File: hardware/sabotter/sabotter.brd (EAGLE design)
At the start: 92.5 x 80 mm, 111 parts, among them IC1 MAX3232CSE, IC2 MAX3232CSE, IC3 OKI-78SR-3.3/1.5-W36H-C, IC4 OKI-78SR-5/1.5-W36H-C, IC6 ATXMEGA256A3U-AU, IC7 LM4871M

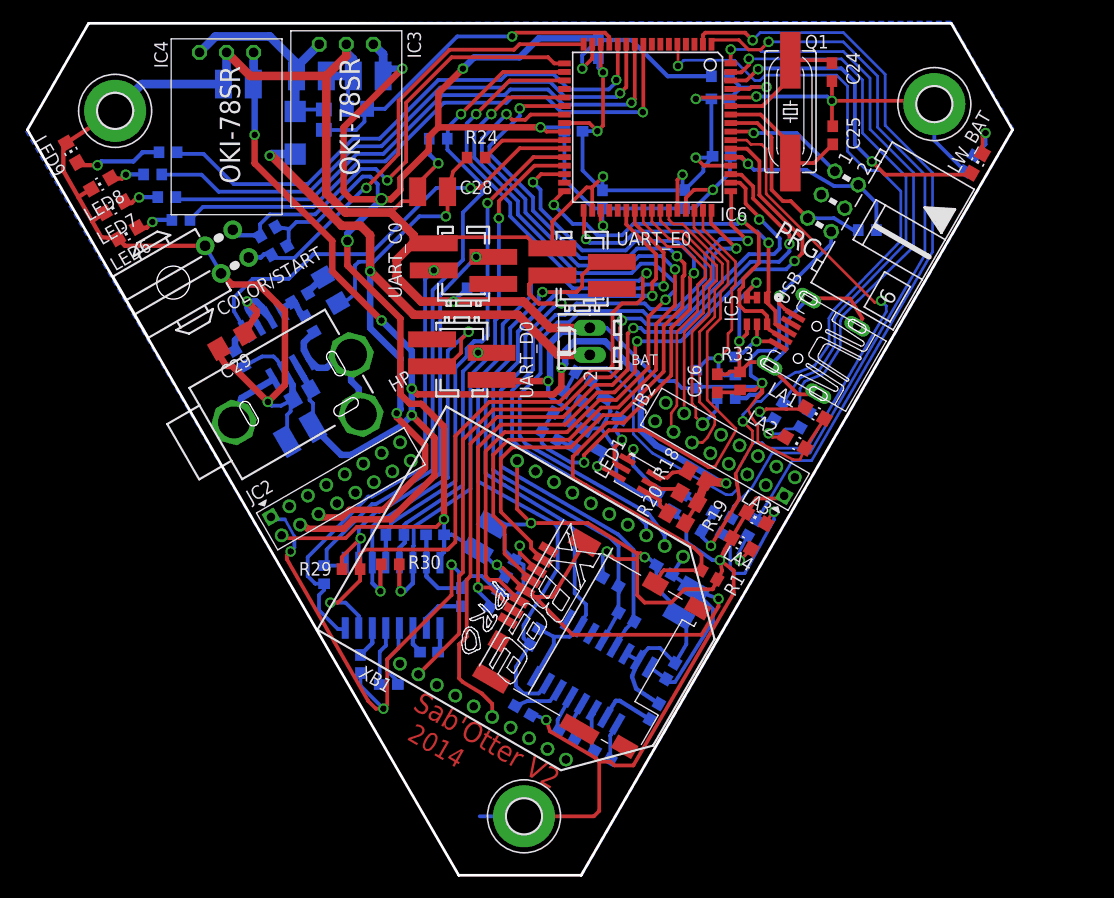
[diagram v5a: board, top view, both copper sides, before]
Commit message: sabotter: uart modified after Jdam  peer review
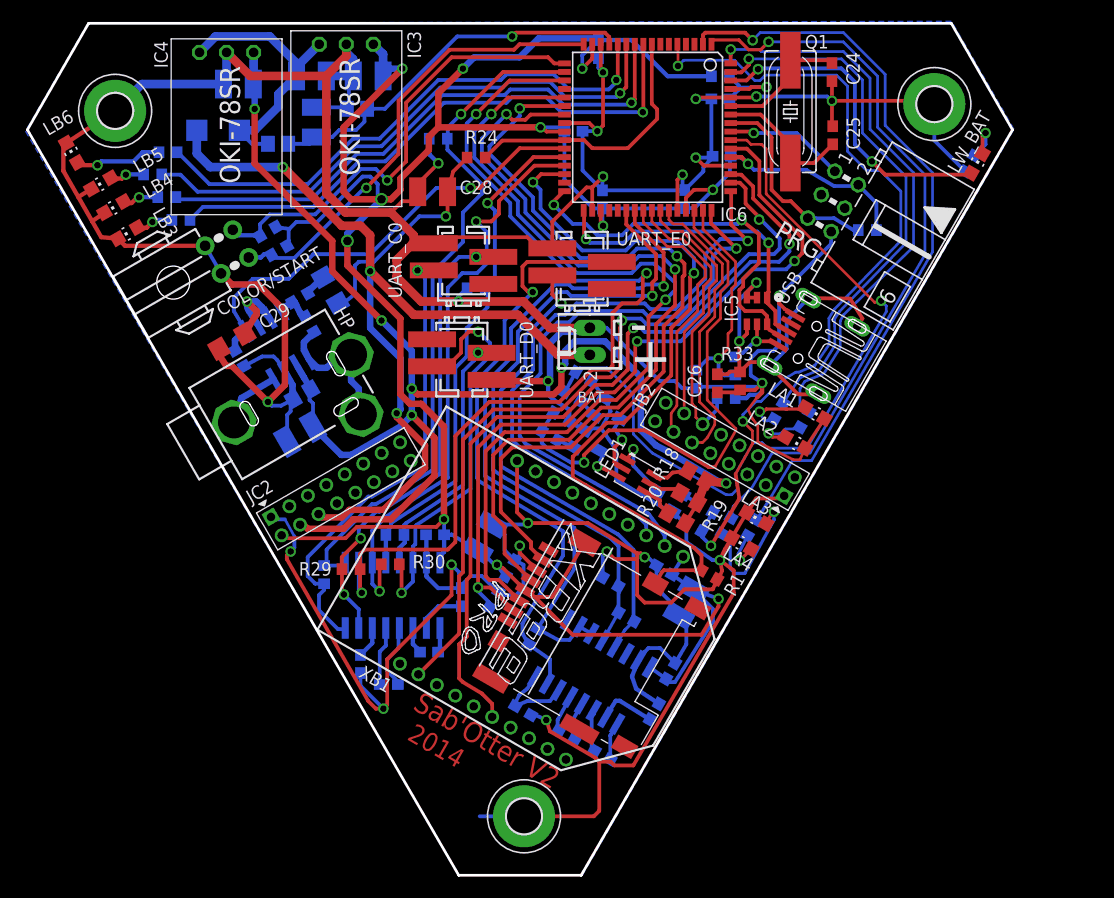
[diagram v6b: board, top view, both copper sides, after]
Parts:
- added C32: C_10UF, robotter_capacitor:C1210
- R24: value 10K-F -> 470
- R33: value (none) -> 10M
- T1, T2, T3: value (none) -> 2n2222
- moved D1 7.24 mm to (17.9, 70.0), turned to 0 degrees
- moved R23 4.87 mm to (23.5, 68.7), turned to 0 degrees
- moved R31 0.12 mm to (47.5, 22.4), turned to 120 degrees
- turned R30 to 180 degrees
- renumbered LED6 to LB3, LED7 to LB4, LED8 to LB5, LED9 to LB6
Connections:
- removed net N$19: C10.1, IC1.6
- removed net PD4: JB2.9
- removed net PD5: JB2.10
- removed net PD6: JB2.8
- removed net PD7: JB2.7
- new net V-: C10.1, IC1.6, IC1.8
- net AUDIO_PWM_3V3: now also IC6.8
- net GND: now also C32.2; no longer IC1.14
- net TX_C0_232: now also IC2.7; no longer IC2.10
- net TX_C0_3V3: now also IC2.10; no longer IC2.7
- net TX_D0_232: now also IC2.14; no longer IC2.11
- net TX_D0_3V3: now also IC2.11; no longer IC2.14
- net TX_E0_232: now also IC1.7; no longer IC1.10, IC1.8
- net TX_E0_3V3: now also IC1.10, IC1.11; no longer IC1.7
- net VBAT_0_1V: now also C32.1
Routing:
- net AUDIO_PWM_3V3: track 8.13 -> 25.5 mm
- net V-: track 0.00 -> 8.50 mm
- net +12V: track 75.4 -> 81.9 mm
- net N$62: track 22.0 -> 27.2 mm
- net TX_E0_3V3: track 70.7 -> 65.7 mm
- net TX_C0_232: track 41.1 -> 46.0 mm, vias 2 -> 3
- net N$19: track 4.65 -> 0.00 mm
- net RX_E0_232: track 49.6 -> 45.4 mm
- net VBAT_0_1V: track 32.0 -> 35.9 mm
- net TX_C0_3V3: track 95.1 -> 91.3 mm
- net TX_D0_3V3: track 51.4 -> 55.2 mm
- net GND: track 583.1 -> 584.8 mm
- net TX_E0_232: track 55.8 -> 57.4 mm
- net TX_D0_232: track 37.5 -> 38.3 mm
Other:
- board text added: "+"
- board text added: "-"

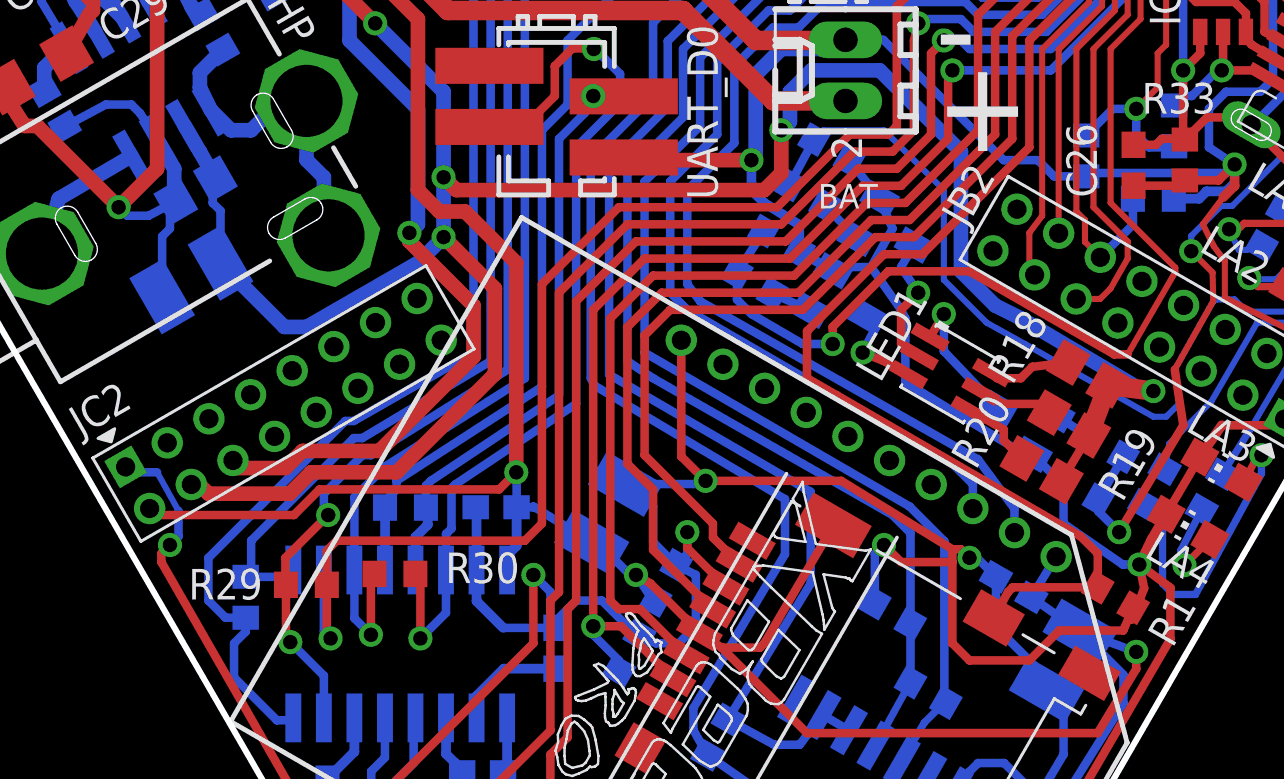
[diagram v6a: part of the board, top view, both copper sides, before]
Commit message: radiospares part number added
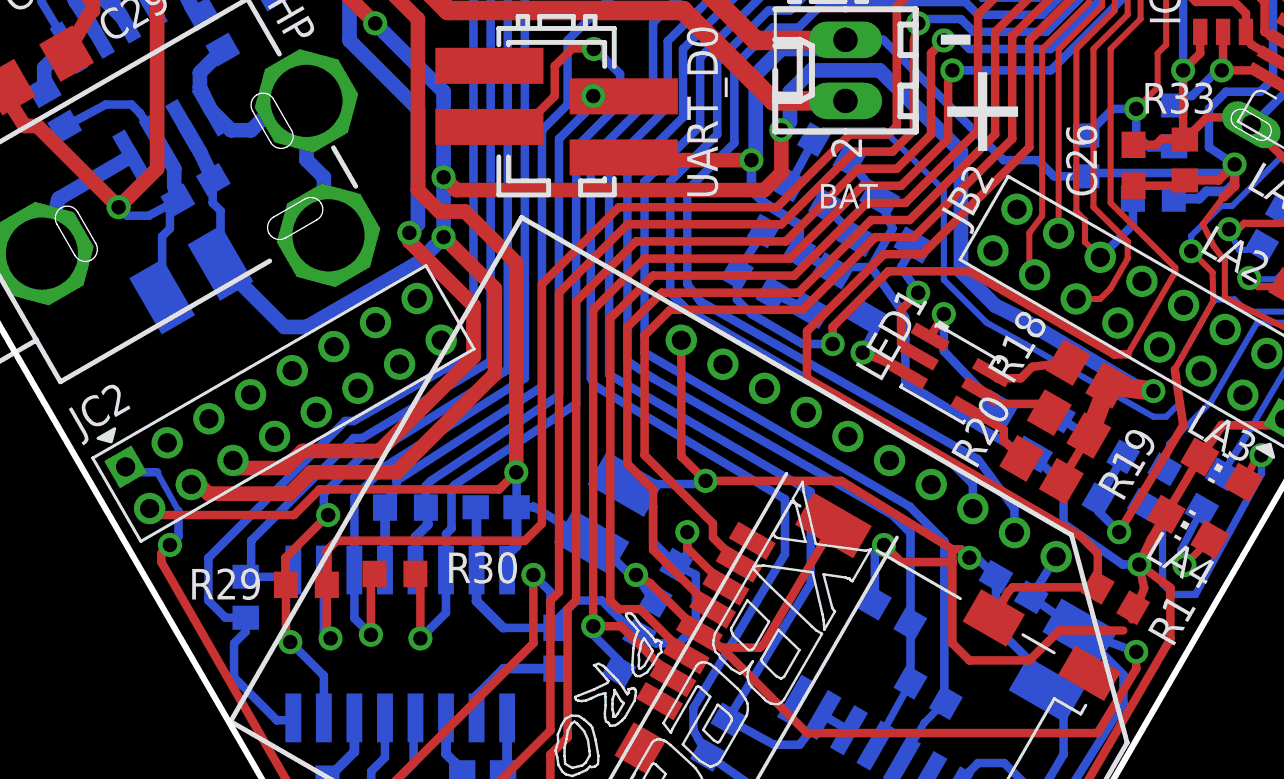
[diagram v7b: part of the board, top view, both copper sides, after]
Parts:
- C13: value 10UFC -> 10µF 35V
- C14, C15, C16, C2: value 10UFC -> 10UF-C_25V
- C28, C30, C32: value C_10UF -> 10UF-C_25V
- C31: value 100NF_50V_0805 -> 100nF_0603_50V; device robotter_capacitor:C0805 -> robotter_capacitor:C0603
- D1: device diode:SMA -> robotter_diode:SMA
- USB: device con-hirose:UX60-MB-5S8 -> robotter_connector:UX60-MB-5S8
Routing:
- net GND: track 584.8 -> 583.5 mm

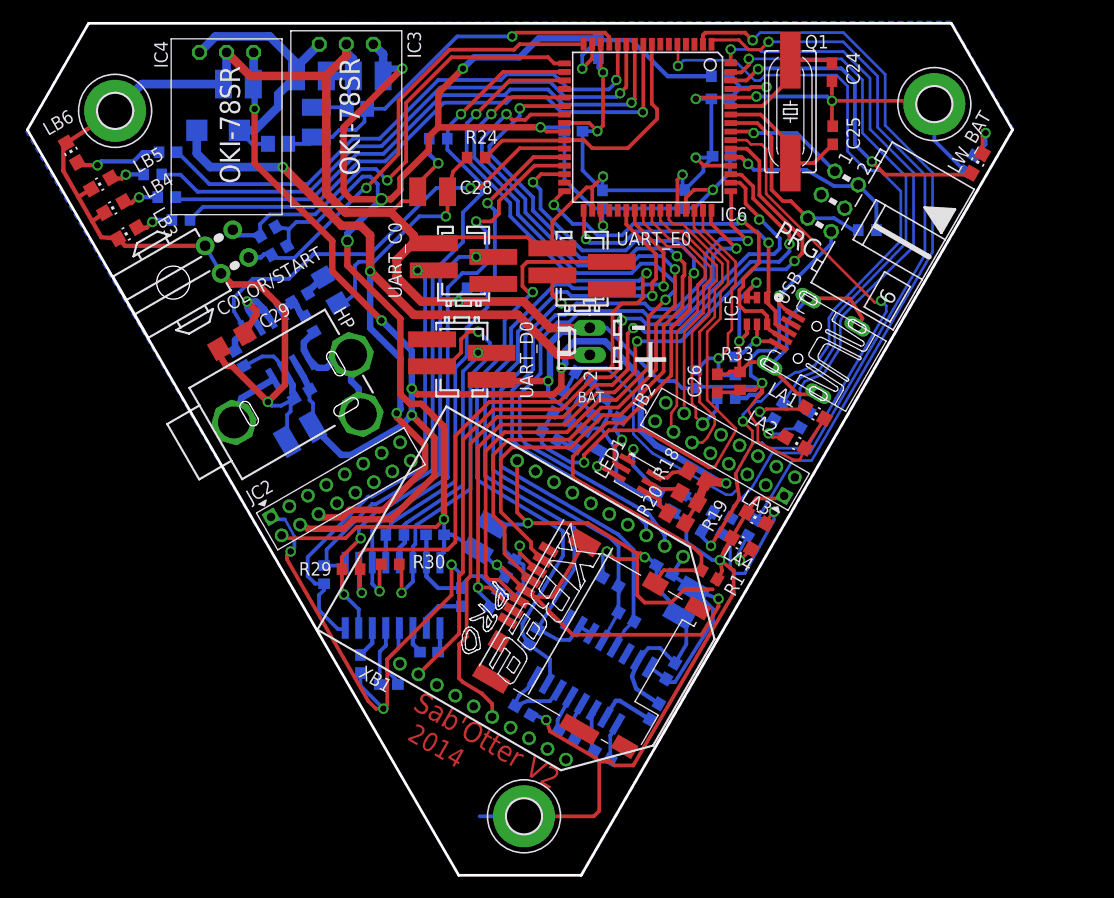
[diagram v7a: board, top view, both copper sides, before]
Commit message: sabotter/sabotter.sch
footprint correction
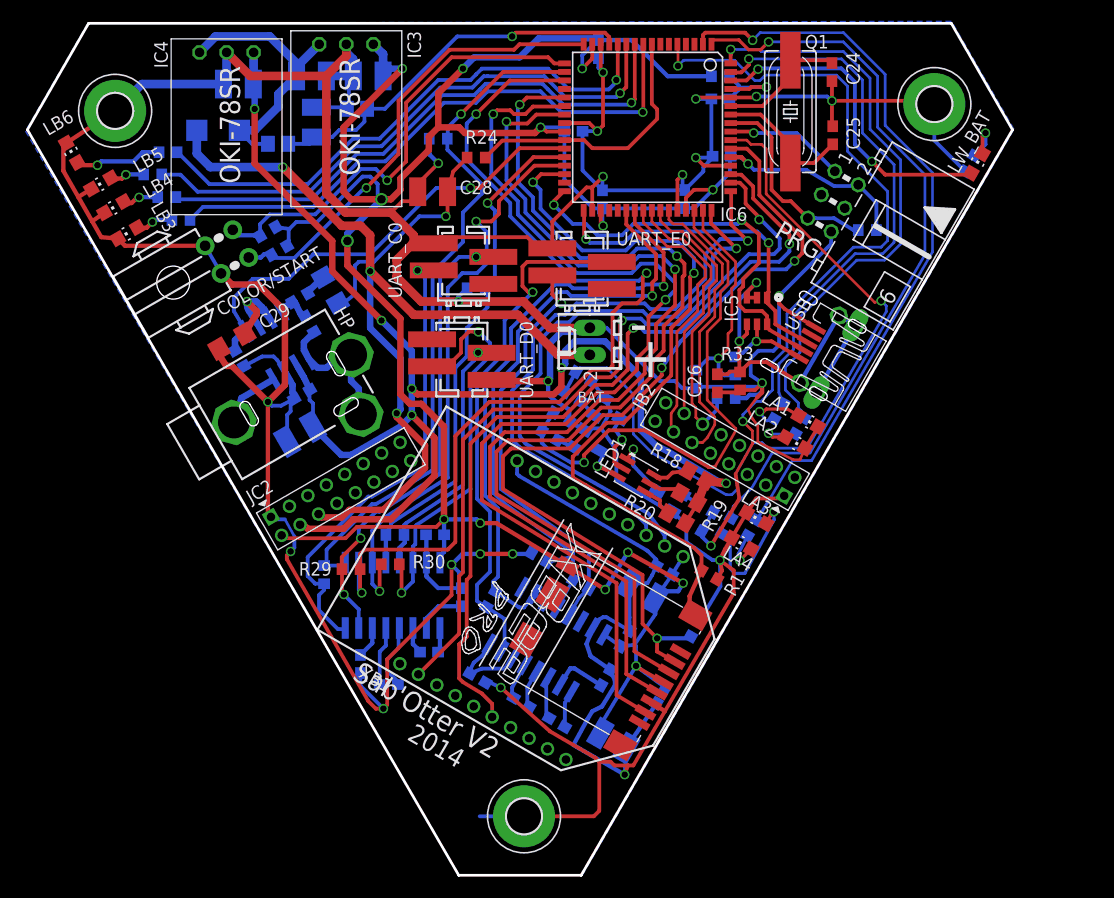
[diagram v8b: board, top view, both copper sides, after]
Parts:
- SD1: value 49225-0821 -> DM3CS-SF; device robotter_connector:49225-0821 -> robotter_connector:DM3CS-SF
- moved C2 22.6 mm to (55.0, 12.6), turned to 210 degrees
- moved R34 19.1 mm to (62.7, 23.2)
- moved C1 18.5 mm to (59.5, 16.9), turned to 300 degrees
- moved SD1 14.6 mm to (48.1, 24.9), turned to 240 degrees
- moved R41 7.08 mm to (48.1, 29.8)
- moved C11 5.58 mm to (54.3, 18.6)
- moved R31 5.29 mm to (43.5, 25.9)
- moved C3 5.24 mm to (56.1, 22.2)
- moved IC1 5.24 mm to (48.8, 22.1)
- moved C4 5.24 mm to (49.7, 14.3)
- moved C10 5.24 mm to (42.3, 18.5)
- moved C5 5.24 mm to (46.4, 16.3)
- moved R26 5.24 mm to (52.0, 27.3)
- moved C16 4.25 mm to (57.8, 26.7), turned to 30 degrees
- moved LA1 0.98 mm to (73.3, 42.6)
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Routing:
- net SD_MISO_3V3: track 74.5 -> 96.9 mm
- net SD_SCLK_3V3: track 76.7 -> 92.3 mm
- net SD_MOSI_3V3: track 80.8 -> 91.2 mm
- net GND: track 583.5 -> 592.6 mm, vias 23 -> 22
- net SD_CS_3V3: track 72.7 -> 81.6 mm
- net TX_E0_3V3: track 65.7 -> 57.1 mm
- net TX_E0_232: track 57.4 -> 50.0 mm
- net RX_E0_232: track 45.4 -> 39.7 mm
- net RX_E0_3V3: track 60.9 -> 57.8 mm
- net USB_5V: track 6.34 -> 8.59 mm
- net USB_DATA+: track 30.2 -> 32.4 mm
- net USB_DATA-: track 36.5 -> 38.7 mm
- net GND1: track 41.1 -> 38.9 mm
- net +3V3: track 269.8 -> 268.1 mm, vias 12 -> 15
- net LA2_3V3: track 53.7 -> 55.4 mm
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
